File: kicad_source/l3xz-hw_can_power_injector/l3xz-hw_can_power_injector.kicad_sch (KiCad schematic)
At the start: 42 parts, among them CN1 Conn_01x02, CN2 Conn_01x04, CN3 Conn_01x04, CN4 Conn_01x02, CN5 Conn_01x04, CN6 Conn_01x04, CN7 Conn_01x02, U1 RAA211650

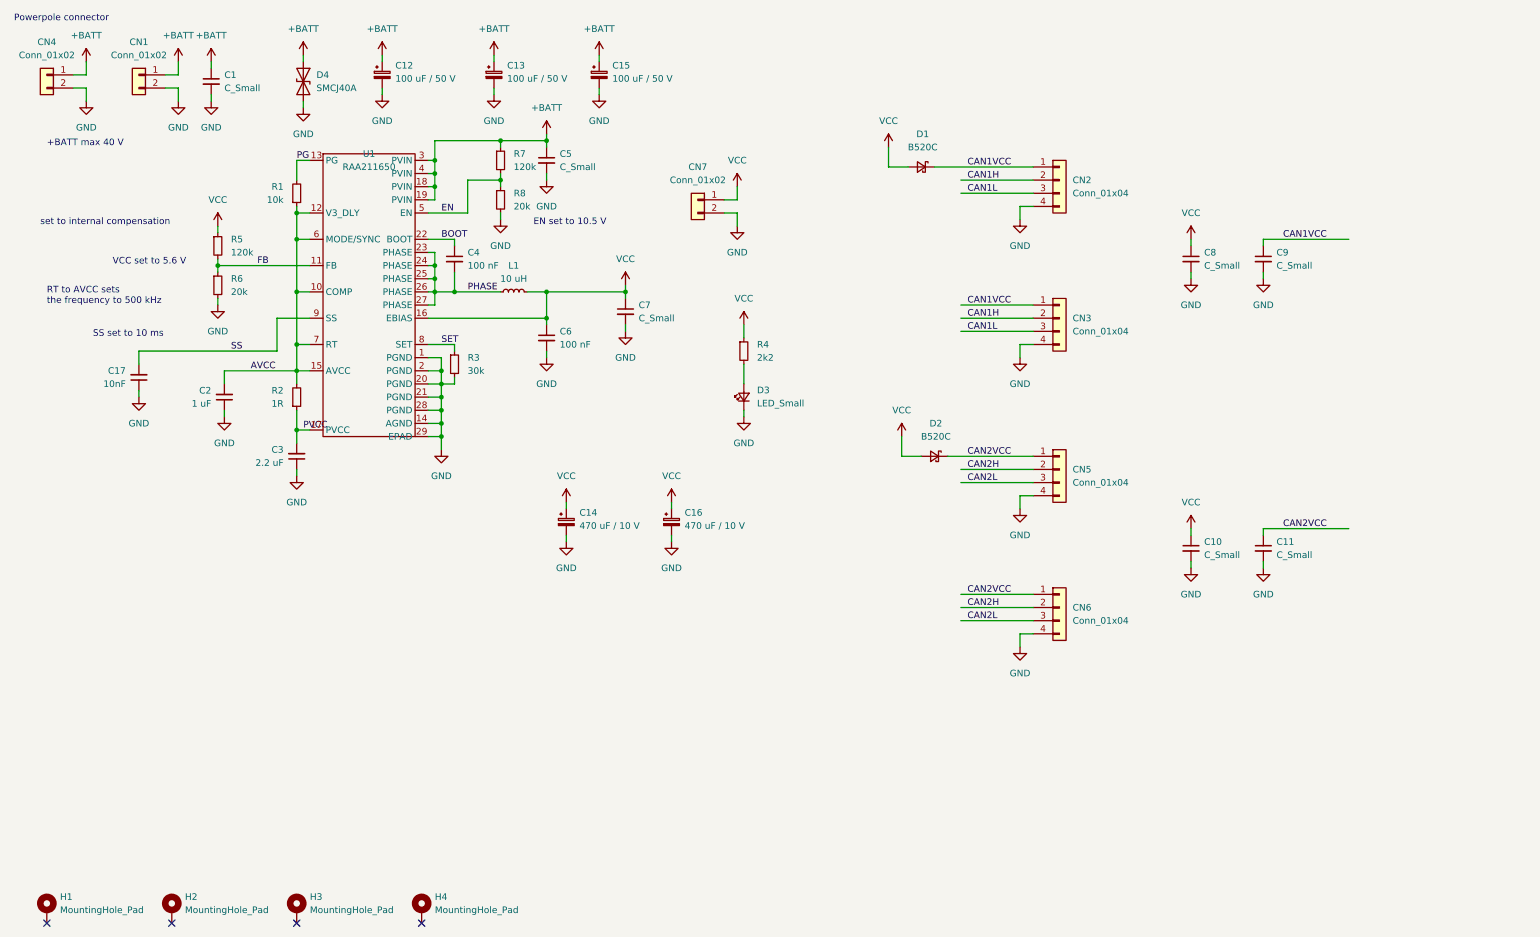
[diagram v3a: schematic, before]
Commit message: updated some component values
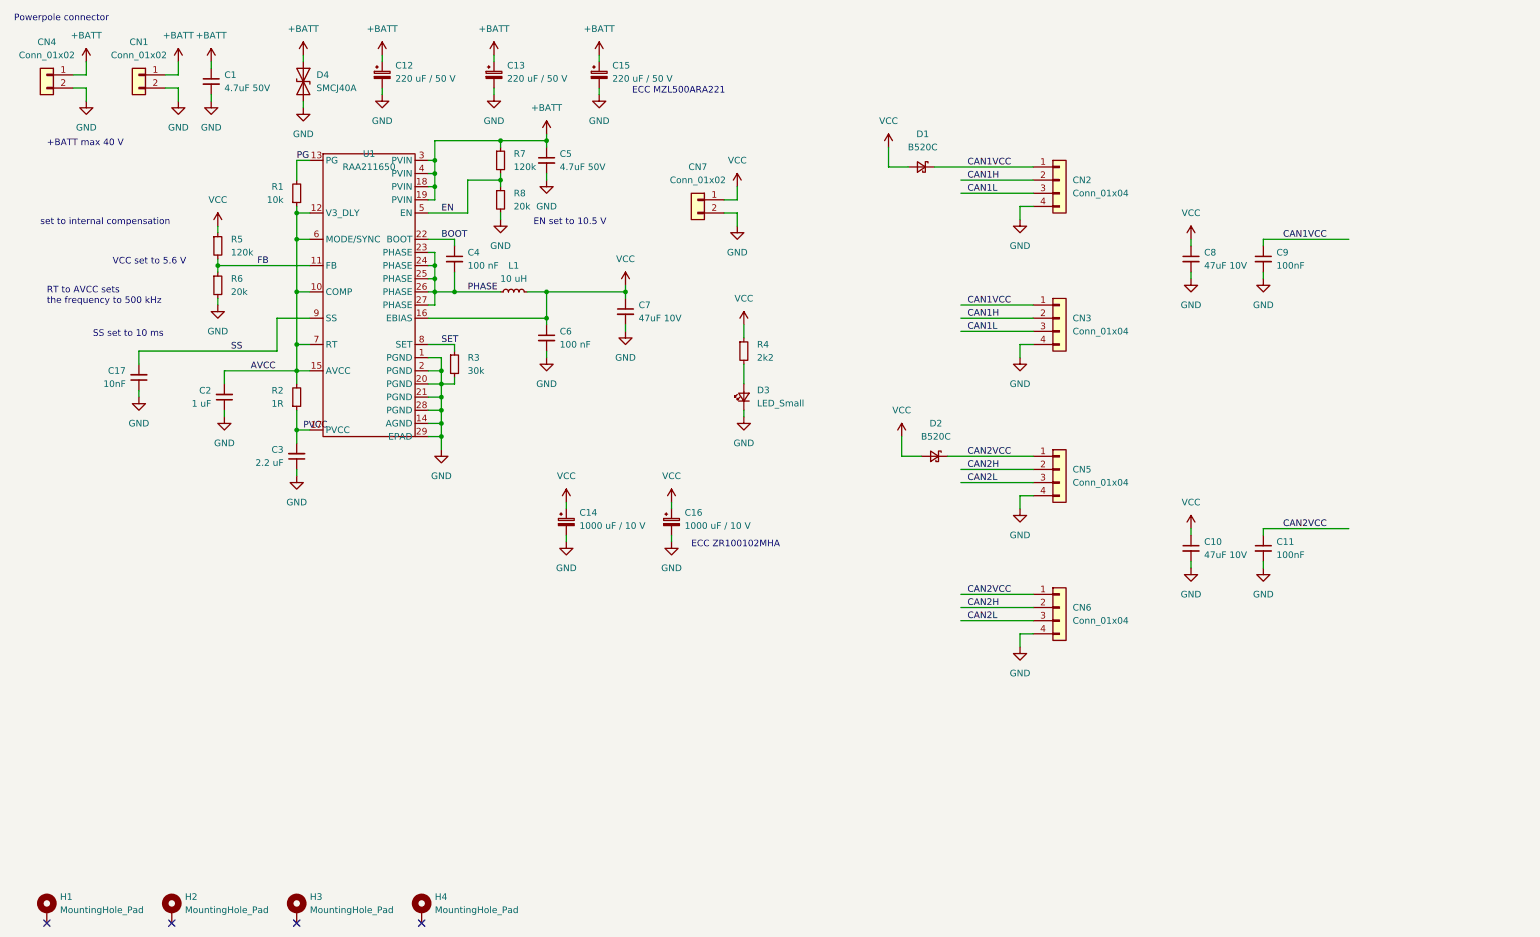
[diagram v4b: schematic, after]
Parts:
- C1, C5: value C_Small -> 4.7uF 50V
- C10, C7, C8: value C_Small -> 47uF 10V
- C11, C9: value C_Small -> 100nF
- C12, C13, C15: value 100 uF / 50 V -> 220 uF / 50 V
- C14, C16: value 470 uF / 10 V -> 1000 uF / 10 V
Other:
- note added: "ECC MZL500ARA221"
- note added: "ECC ZR100102MHA"
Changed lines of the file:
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@@
+    (effects (font (size 1.27 1.27)) (justify left bottom))
+  )
+  (text "ECC ZR100102MHA" (at 146.05 119.38 0)
     (effects (font (size 1.27 1.27)) (justify left bottom))
   )
   (text "set to internal compensation" (at 20.32 57.15 0)
+    (effects (font (size 1.27 1.27)) (justify left bottom))
+  )
+  (text "ECC MZL500ARA221" (at 134.62 31.75 0)
     (effects (font (size 1.27 1.27)) (justify left bottom))
   )
@@
       (effects (font (size 1.27 1.27)) (justify left))
     )
-    (property "Value" "C_Small" (id 1) (at 120.65 45.7262 0)
+    (property "Value" "4.7uF 50V" (id 1) (at 120.65 45.7262 0)
       (effects (font (size 1.27 1.27)) (justify left))
     )
@@
       (effects (font (size 1.27 1.27)) (justify left))
     )
-    (property "Value" "100 uF / 50 V" (id 1) (at 110.49 28.6638 0)
+    (property "Value" "220 uF / 50 V" (id 1) (at 110.49 28.6638 0)
       (effects (font (size 1.27 1.27)) (justify left))
     )
@@
       (effects (font (size 1.27 1.27)) (justify left))
     )
-    (property "Value" "100 uF / 50 V" (id 1) (at 130.81 28.6638 0)
+    (property "Value" "220 uF / 50 V" (id 1) (at 130.81 28.6638 0)
       (effects (font (size 1.27 1.27)) (justify left))
     )
@@
       (effects (font (size 1.27 1.27)) (justify left))
     )
-    (property "Value" "C_Small" (id 1) (at 259.08 64.7762 0)
+    (property "Value" "100nF" (id 1) (at 259.08 64.7762 0)
       (effects (font (size 1.27 1.27)) (justify left))
     )
@@
       (effects (font (size 1.27 1.27)) (justify left))
     )
-    (property "Value" "C_Small" (id 1) (at 245.11 120.6562 0)
+    (property "Value" "47uF 10V" (id 1) (at 245.11 120.6562 0)
       (effects (font (size 1.27 1.27)) (justify left))
     )
@@
       (effects (font (size 1.27 1.27)) (justify left))
     )
-    (property "Value" "C_Small" (id 1) (at 135.89 74.9362 0)
+    (property "Value" "47uF 10V" (id 1) (at 135.89 74.9362 0)
       (effects (font (size 1.27 1.27)) (justify left))
     )
@@
       (effects (font (size 1.27 1.27)) (justify left))
     )
-    (property "Value" "C_Small" (id 1) (at 55.88 30.4862 0)
+    (property "Value" "4.7uF 50V" (id 1) (at 55.88 30.4862 0)
       (effects (font (size 1.27 1.27)) (justify left))
     )
@@
       (effects (font (size 1.27 1.27)) (justify left))
     )
-    (property "Value" "100 uF / 50 V" (id 1) (at 88.9 28.6638 0)
+    (property "Value" "220 uF / 50 V" (id 1) (at 88.9 28.6638 0)
       (effects (font (size 1.27 1.27)) (justify left))
     )
@@
       (effects (font (size 1.27 1.27)) (justify left))
     )
-    (property "Value" "C_Small" (id 1) (at 259.08 120.6562 0)
+    (property "Value" "100nF" (id 1) (at 259.08 120.6562 0)
       (effects (font (size 1.27 1.27)) (justify left))
     )
@@
       (effects (font (size 1.27 1.27)) (justify left))
     )
-    (property "Value" "C_Small" (id 1) (at 245.11 64.7762 0)
+    (property "Value" "47uF 10V" (id 1) (at 245.11 64.7762 0)
       (effects (font (size 1.27 1.27)) (justify left))
     )
@@
       (effects (font (size 1.27 1.27)) (justify left))
     )
-    (property "Value" "470 uF / 10 V" (id 1) (at 124.46 115.0238 0)
+    (property "Value" "1000 uF / 10 V" (id 1) (at 124.46 115.0238 0)
       (effects (font (size 1.27 1.27)) (justify left))
     )
@@
       (effects (font (size 1.27 1.27)) (justify left))
     )
-    (property "Value" "470 uF / 10 V" (id 1) (at 144.78 115.0238 0)
+    (property "Value" "1000 uF / 10 V" (id 1) (at 144.78 115.0238 0)
       (effects (font (size 1.27 1.27)) (justify left))
     )
@@
     )
     (path "/5fed680c-7375-4ebc-bb86-a241d3c8e39a"
-      (reference "C1") (unit 1) (value "C_Small") (footprint "Capacitor_SMD:C_1210_3225Metric")
+      (reference "C1") (unit 1) (value "4.7uF 50V") (footprint "Capacitor_SMD:C_1210_3225Metric")
     )
     (path "/01b9b56c-9745-4e02-a283-e3a2b7aa9655"
@@
     )
     (path "/0a83da60-08d9-458b-b787-1e44114969b4"
-      (reference "C5") (unit 1) (value "C_Small") (footprint "Capacitor_SMD:C_1210_3225Metric")
+      (reference "C5") (unit 1) (value "4.7uF 50V") (footprint "Capacitor_SMD:C_1210_3225Metric")
     )
     (path "/14fdad3c-45b4-4709-9713-c612c909f90b"
@@
     )
     (path "/56a10a95-bfe6-4198-a885-eb1c51ed4a80"
-      (reference "C7") (unit 1) (value "C_Small") (footprint "Capacitor_SMD:C_1210_3225Metric")
+      (reference "C7") (unit 1) (value "47uF 10V") (footprint "Capacitor_SMD:C_1210_3225Metric")
     )
     (path "/9ceda24a-2190-448e-a9f0-7902ecae7458"
-      (reference "C8") (unit 1) (value "C_Small") (footprint "Capacitor_SMD:C_1210_3225Metric")
+      (reference "C8") (unit 1) (value "47uF 10V") (footprint "Capacitor_SMD:C_1210_3225Metric")
     )
     (path "/40fd1244-d027-4abc-a17d-3da295028d0c"
-      (reference "C9") (unit 1) (value "C_Small") (footprint "Capacitor_SMD:C_0603_1608Metric")
+      (reference "C9") (unit 1) (value "100nF") (footprint "Capacitor_SMD:C_0603_1608Metric")
     )
     (path "/4b87a511-f1ff-403b-82bb-48a1b6d84d3c"
-      (reference "C10") (unit 1) (value "C_Small") (footprint "Capacitor_SMD:C_1210_3225Metric")
+      (reference "C10") (unit 1) (value "47uF 10V") (footprint "Capacitor_SMD:C_1210_3225Metric")
     )
     (path "/8263f46b-91e2-4edf-a9b1-dab669402431"
-      (reference "C11") (unit 1) (value "C_Small") (footprint "Capacitor_SMD:C_0603_1608Metric")
+      (reference "C11") (unit 1) (value "100nF") (footprint "Capacitor_SMD:C_0603_1608Metric")
     )
     (path "/8150ddc6-6836-42ce-9cdd-33fbb4f9853f"
-      (reference "C12") (unit 1) (value "100 uF / 50 V") (footprint "Capacitor_SMD:CP_Elec_10x10")
+      (reference "C12") (unit 1) (value "220 uF / 50 V") (footprint "Capacitor_SMD:CP_Elec_10x10")
     )
     (path "/2b760b58-9d66-4f19-b02f-f514e937b10d"
-      (reference "C13") (unit 1) (value "100 uF / 50 V") (footprint "Capacitor_SMD:CP_Elec_10x10")
+      (reference "C13") (unit 1) (value "220 uF / 50 V") (footprint "Capacitor_SMD:CP_Elec_10x10")
     )
     (path "/d079dd89-f453-467a-bcd2-c684b6b9845c"
-      (reference "C14") (unit 1) (value "470 uF / 10 V") (footprint "Capacitor_SMD:CP_Elec_8x10")
+      (reference "C14") (unit 1) (value "1000 uF / 10 V") (footprint "Capacitor_SMD:CP_Elec_8x10")
     )
     (path "/35099388-2ca1-4fa7-82ae-579674b246d2"
-      (reference "C15") (unit 1) (value "100 uF / 50 V") (footprint "Capacitor_SMD:CP_Elec_10x10")
+      (reference "C15") (unit 1) (value "220 uF / 50 V") (footprint "Capacitor_SMD:CP_Elec_10x10")
     )
     (path "/e7c3b84b-0851-42ba-90cb-e6c399505507"
-      (reference "C16") (unit 1) (value "470 uF / 10 V") (footprint "Capacitor_SMD:CP_Elec_8x10")
+      (reference "C16") (unit 1) (value "1000 uF / 10 V") (footprint "Capacitor_SMD:CP_Elec_8x10")
     )
     (path "/1b346cae-2c1b-4465-97a8-a36b5cf14b51"

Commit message: made drc, corrected some errors, added label
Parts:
- added L2: Label, generationmake:generationmake_small_silk, symbol generationmake:Label
- added L3: Label, generationmake:generationmake_small_solder, symbol generationmake:Label
- CN1, CN7: value Conn_01x02 -> DNI
- CN2, CN3, CN5, CN6: value Conn_01x04 -> SM04B-GHS-TB; footprint Connector_JST:JST_GH_BM04B-GHS-TBT_1x04-1MP_P1.25mm_Vertical -> Connector_JST:JST_GH_SM04B-GHS-TB_1x04-1MP_P1.25mm_Horizontal; symbol Connector_Generic:Conn_01x04 -> Connector_Generic_MountingPin:Conn_01x04_MountingPin
- L1: footprint Inductor_SMD:L_7.3x7.3_H4.5 -> Inductor_SMD:L_Wuerth_HCI-1050
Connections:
- new net MP: CN2.MP (MountPin), CN3.MP (MountPin), CN5.MP (MountPin), CN6.MP (MountPin)
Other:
- note added: "Wuerth 7443251000"

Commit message: updated schematic pdf and images
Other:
- note added: "ECC MZL500ARA221 EMZL500ARA221MJA0G"
- note added: "ECC ZR100102MHA EMZR100ARA102MHA0G"
- note removed: "ECC MZL500ARA221"
- note removed: "ECC ZR100102MHA"
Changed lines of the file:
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@@
     (effects (font (size 1.27 1.27)) (justify left bottom))
   )
-  (text "ECC ZR100102MHA" (at 146.05 119.38 0)
+  (text "ECC ZR100102MHA\nEMZR100ARA102MHA0G" (at 146.05 121.92 0)
     (effects (font (size 1.27 1.27)) (justify left bottom))
   )
@@
     (effects (font (size 1.27 1.27)) (justify left bottom))
   )
-  (text "ECC MZL500ARA221" (at 134.62 31.75 0)
+  (text "ECC MZL500ARA221\nEMZL500ARA221MJA0G" (at 134.62 34.29 0)
     (effects (font (size 1.27 1.27)) (justify left bottom))
   )
